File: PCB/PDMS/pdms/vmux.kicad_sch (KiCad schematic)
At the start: 35 parts, among them IC2 74HC4067PW-Q100J

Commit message: Clean-up of schematics
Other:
- note added: "Output channel voltage measurement mux"
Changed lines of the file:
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@@
     (stroke (width 0) (type default) (color 0 0 0 0))
+  )
+  (text "Output channel voltage measurement mux" (at 99.187 129.159 0)
+    (effects (font (size 2 2) italic) (justify left bottom))
   )
   (label "HP_MOS_DIV7" (at 88.138 54.102 0)

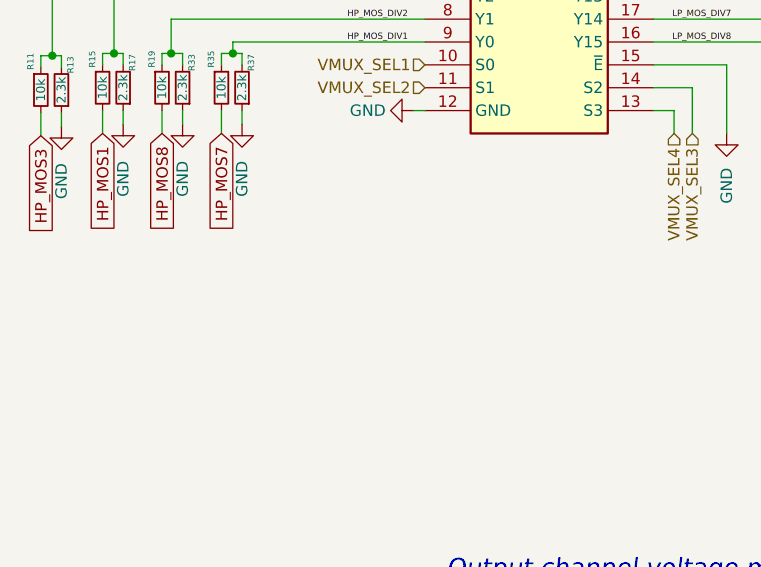
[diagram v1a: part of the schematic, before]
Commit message: Changes after board 4.1 first unit assembly
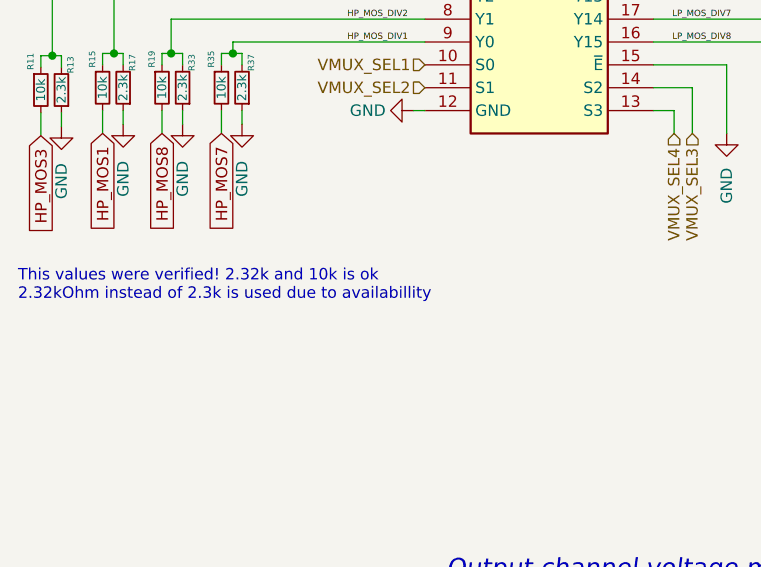
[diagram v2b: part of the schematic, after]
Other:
- note added: "This values were verified! 2.32k and 10k is ok 2.32kOhm instead of 2.3k is used due to availabillity"
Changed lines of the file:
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@@
     (effects (font (size 2 2) italic) (justify left bottom))
+  )
+  (text "This values were verified! 2.32k and 10k is ok\n2.32kOhm instead of 2.3k is used due to availabillity"
+    (at 51.562 98.171 0)
+    (effects (font (size 1.27 1.27)) (justify left bottom))
   )
   (label "HP_MOS_DIV7" (at 88.138 54.102 0)

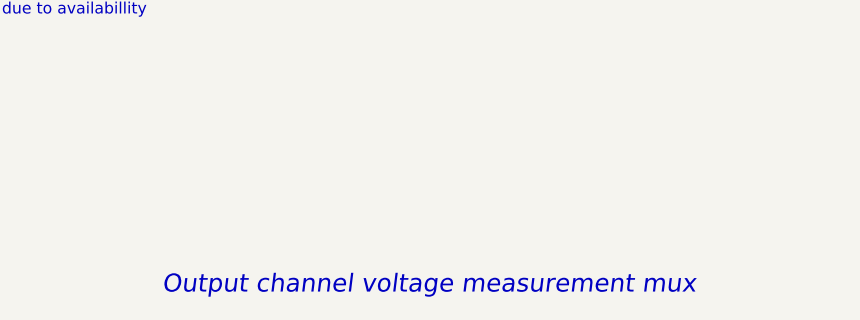
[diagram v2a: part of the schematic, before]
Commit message: WIP PCB folder structure and schematic clean-up
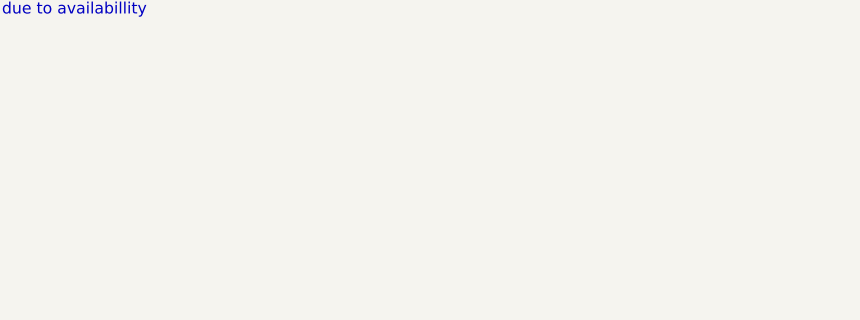
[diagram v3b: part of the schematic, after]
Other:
- note removed: "Output channel voltage measurement mux"
- company: (none) -> PGRacing Team
- title: (none) -> Output channel voltage measurement mux
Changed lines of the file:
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@@
 (kicad_sch (version 20211123) (generator eeschema)
   (paper "A5")
+  (title_block
+    (title "Output channel voltage measurement mux")
+    (rev "V4.2")
+    (company "PGRacing Team")
+    (comment 1 "Karol Pergoł")
+  )
   (junction (at 150.368 50.292) (diameter 0) (color 0 0 0 0)
   )
@@
     (stroke (width 0) (type default) (color 0 0 0 0))
   )
-  (text "Output channel voltage measurement mux" (at 99.187 129.159 0)
-    (effects (font (size 2 2) italic) (justify left bottom))
-  )
   (text "This values were verified! 2.32k and 10k is ok\n2.32kOhm instead of 2.3k is used due to availabillity"

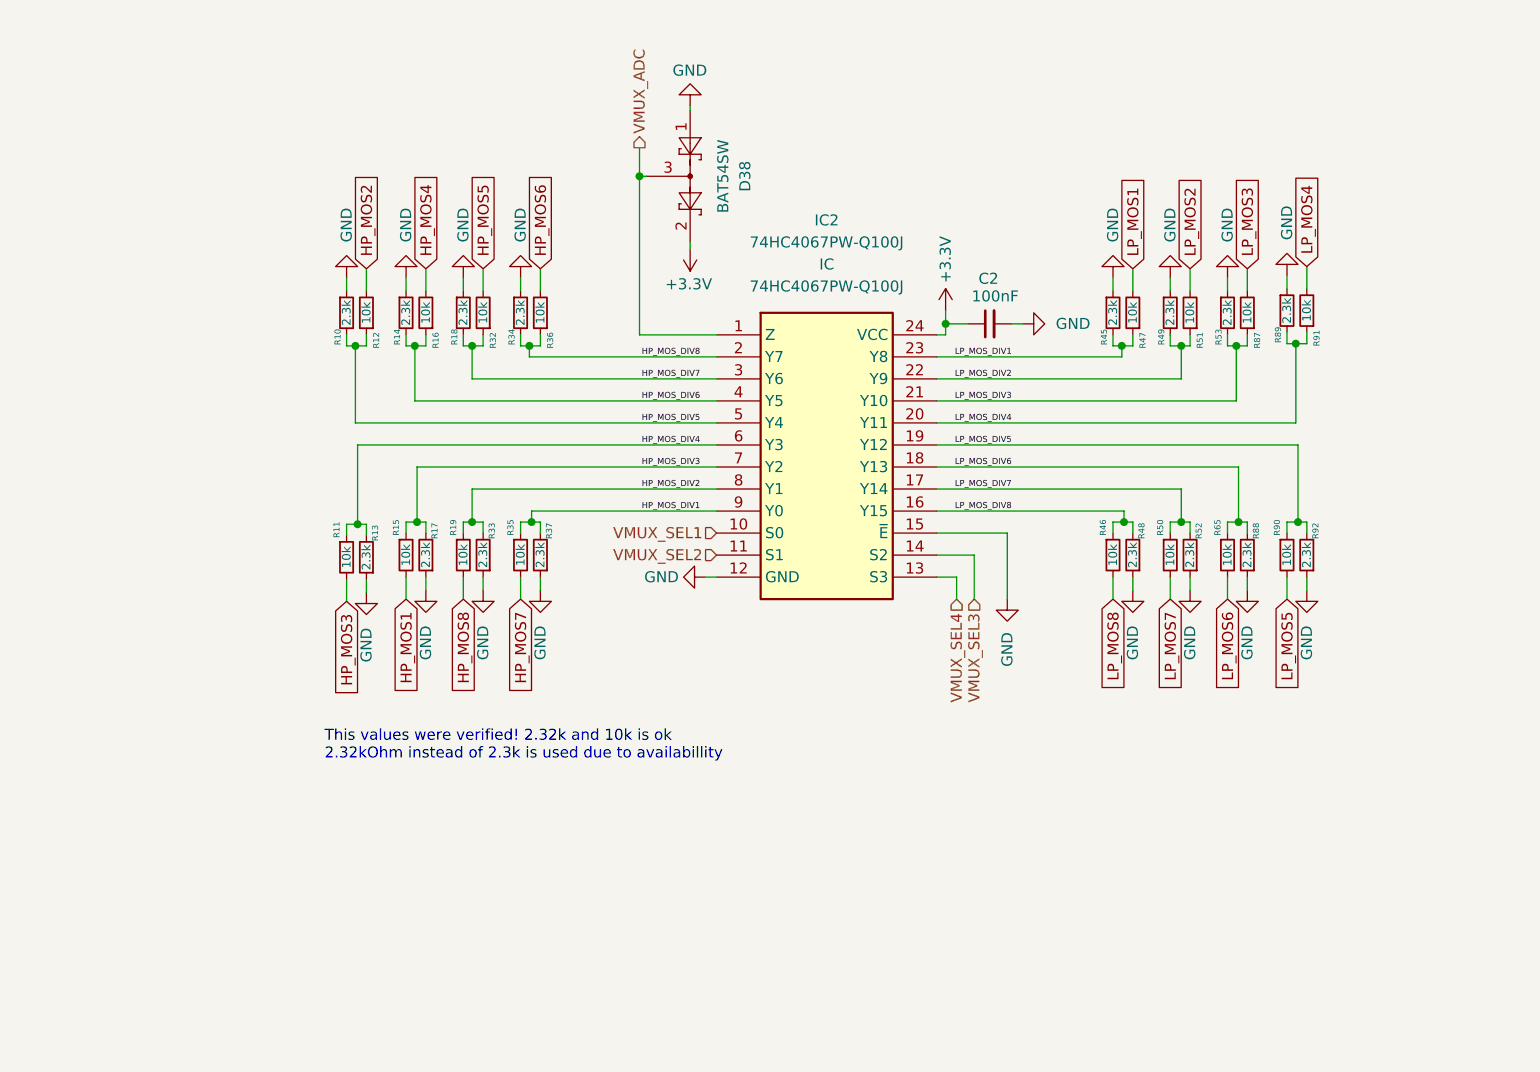
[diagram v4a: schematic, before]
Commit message: PDMS PCB WIP modification - added better input protection and filtering for voltage channels
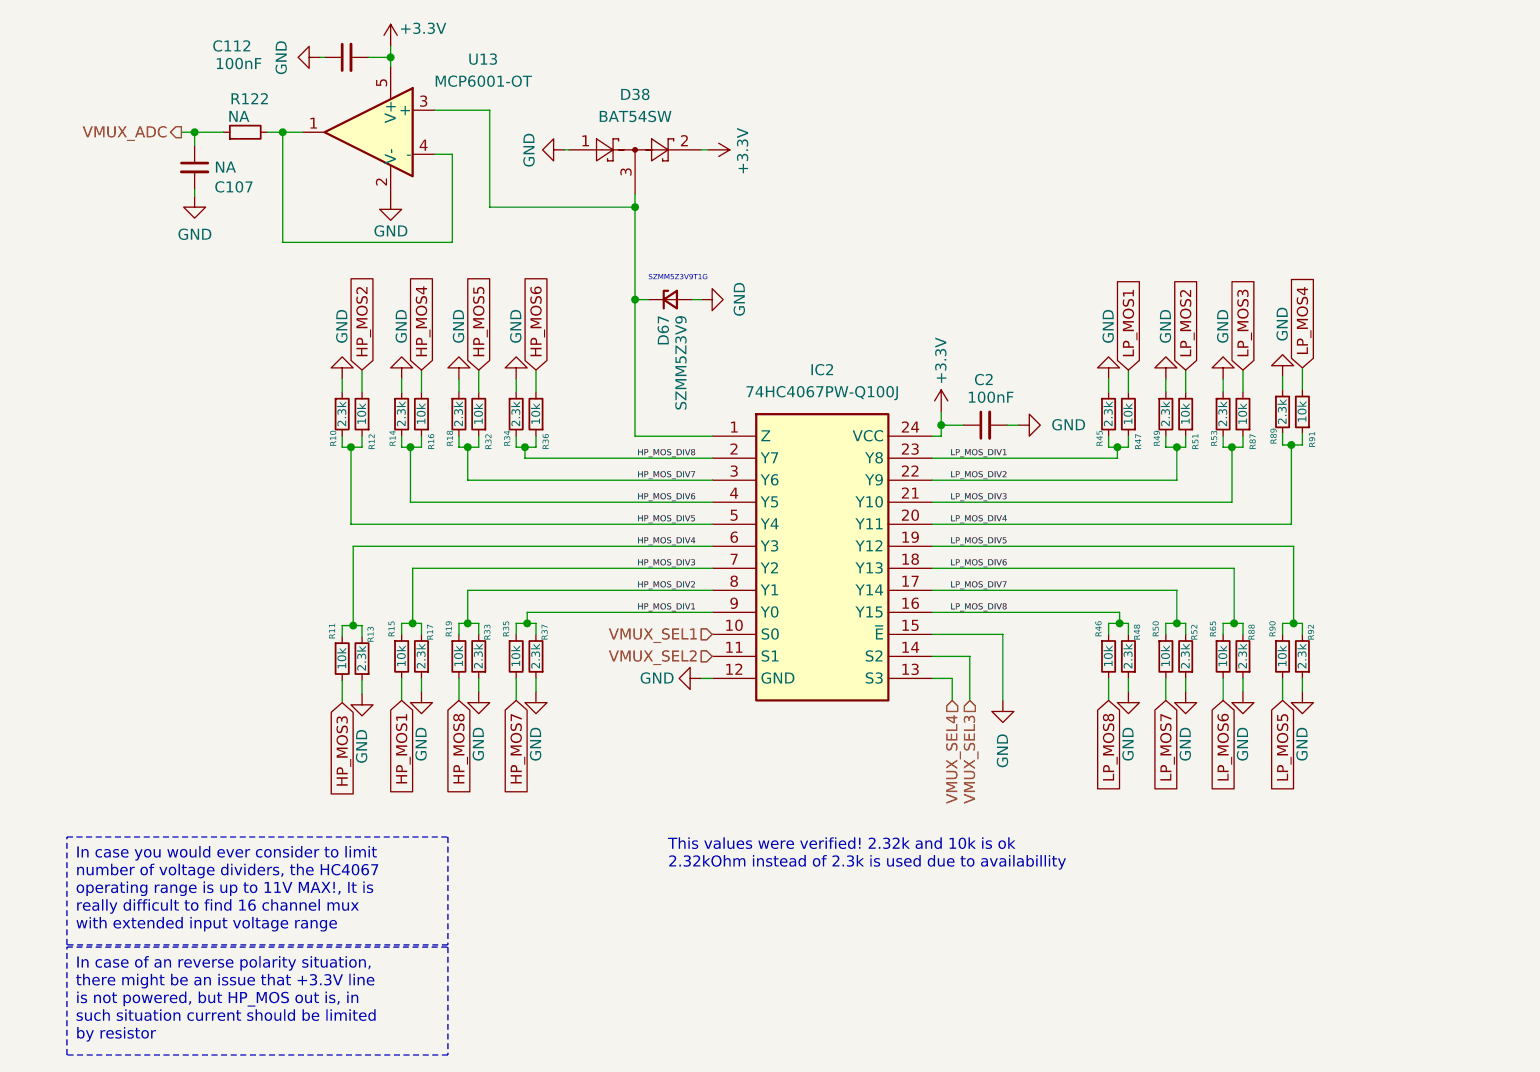
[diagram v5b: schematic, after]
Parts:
- added C107: NA, Capacitor_SMD:C_0402_1005Metric, symbol Device:C_Small
- added C112: 100nF, Capacitor_SMD:C_0402_1005Metric, symbol Device:C_Small
- added D67: SZMM5Z3V9, Diode_SMD:D_SOD-523, symbol Device:D_Zener_Small
- added R122: NA, Resistor_SMD:R_0402_1005Metric, symbol Device:R_Small
- added U13: MCP6001-OT, Package_TO_SOT_SMD:SOT-23-5, symbol Amplifier_Operational:MCP6001-OT
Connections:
- net +3.3V: now also C112.2, U13.5 (V+)
- net GND: now also C107.2, C112.1, D67.2 (A), U13.2 (V-)
- net VMUX_ADC: now also C107.1, R122.1; no longer D38.3, IC2.1 (Z)
- new net: R122.2, U13.1, U13.4 (-)
- new net: D38.3, D67.1 (K), IC2.1 (Z), U13.3 (+)
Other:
- note added: "SZMM5Z3V9T1G"
- moved on the sheet: C2, D38, IC2, R10, R11, R12, R13, R14, R15, R16, R17, R18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

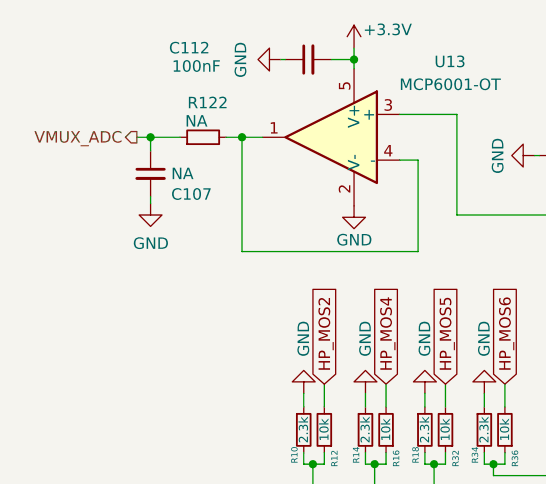
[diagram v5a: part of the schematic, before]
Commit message: Added gerbers of PDMS v4.3, assembly docs, modified DNP parameters
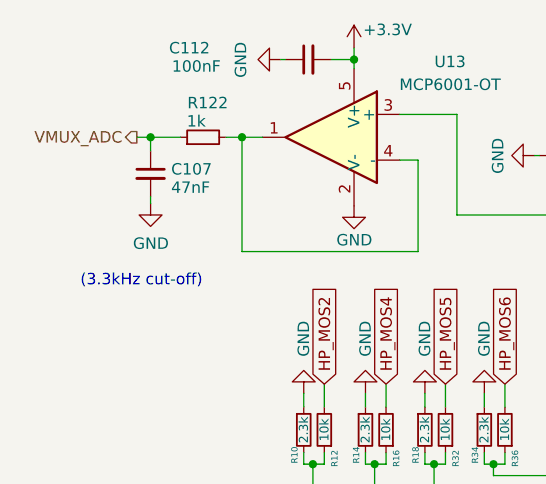
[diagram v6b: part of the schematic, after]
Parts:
- C107: value NA -> 47nF
- R122: value NA -> 1k
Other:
- note added: "(3.3kHz cut-off)"
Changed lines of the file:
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@@
 		)
 	)
+	(text "(3.3kHz cut-off)"
+		(exclude_from_sim no)
+		(at 35.56 41.656 0)
+		(effects
+			(font
+				(size 1.27 1.27)
+				(color 255 0 255 1)
+			)
+		)
+	)
 	(label "HP_MOS_DIV7"
 		(at 87.63 65.786 0)
@@
 			)
 		)
-		(property "Value" "NA"
+		(property "Value" "1k"
 			(at 41.656 23.876 90)
 			(effects
@@
 		(dnp no)
 		(property "Reference" "C107"
-			(at 38.862 32.004 0)
+			(at 38.862 29.21 0)
 			(effects
 				(font
@@
 			)
 		)
-		(property "Value" "NA"
-			(at 38.862 29.718 0)
+		(property "Value" "47nF"
+			(at 38.862 31.242 0)
 			(effects
 				(font

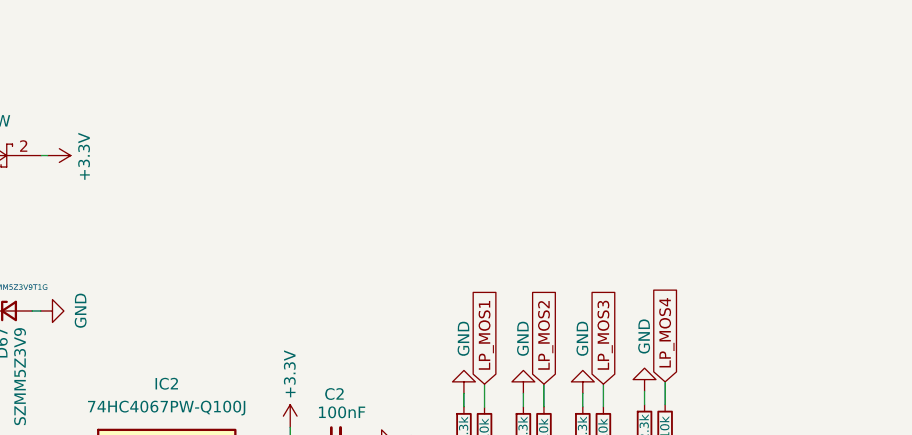
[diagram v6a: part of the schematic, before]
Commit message: Marked changes and notes for future PCB, anti-aliasing filter cacitors soldered on top of vmux divider, DEN should be controlled via IN, so no open-circuit is detected during PWM
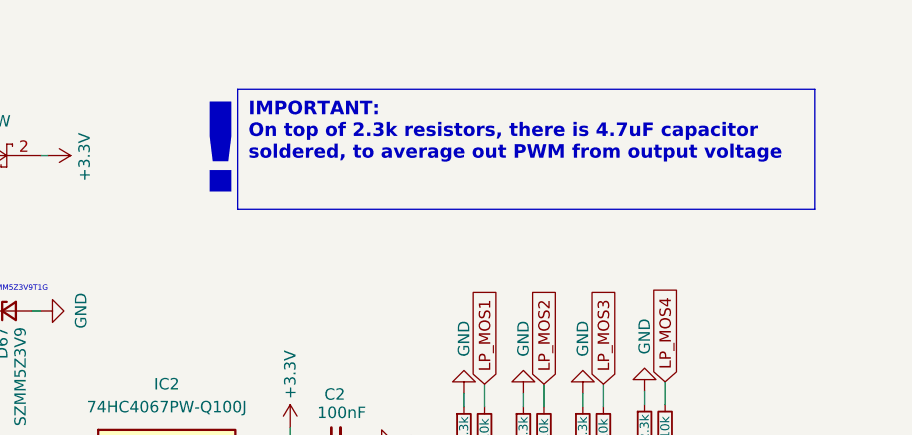
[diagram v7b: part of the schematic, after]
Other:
- note added: "!"
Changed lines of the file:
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@@
+		)
+	)
+	(text_box "IMPORTANT: \nOn top of 2.3k resistors, there is 4.7uF capacitor soldered, to average out PWM from output voltage"
+		(exclude_from_sim no)
+		(at 116.84 20.32 0)
+		(size 64.135 13.335)
+		(stroke
+			(width 0)
+			(type default)
+			(color 255 0 255 1)
+		)
+		(fill
+			(type none)
+		)
+		(effects
+			(font
+				(size 1.5 1.5)
+				(thickness 0.3)
+				(bold yes)
+				(color 255 0 255 1)
+			)
+			(justify left top)
 		)
 	)
@@
 		)
 	)
+	(text "!"
+		(exclude_from_sim no)
+		(at 114.935 27.305 0)
+		(effects
+			(font
+				(size 10 10)
+				(thickness 0.6)
+				(bold yes)
+				(color 255 0 255 1)
+			)
+		)
+	)
